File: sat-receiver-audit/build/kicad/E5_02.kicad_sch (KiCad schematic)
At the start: 18 parts, among them J502 UART5 console 3pin locking, J504 Olimex GX16-4 IMU DESIGN pino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, J505 LAB BUS 6pin locking DESIGN, J520 Q6A HDMI Type-A existing port, J522 Q6A factory EDL button functi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, J550 IMU pack cable termination DE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, SW501 EDL recessed momentary NO, U506 LM66100DCKR HDMI5V ideal diode, U520 Wisecoco display/controller a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, U551 TPD4E1U06DBVR, U552 TPD4E1U06DBVR

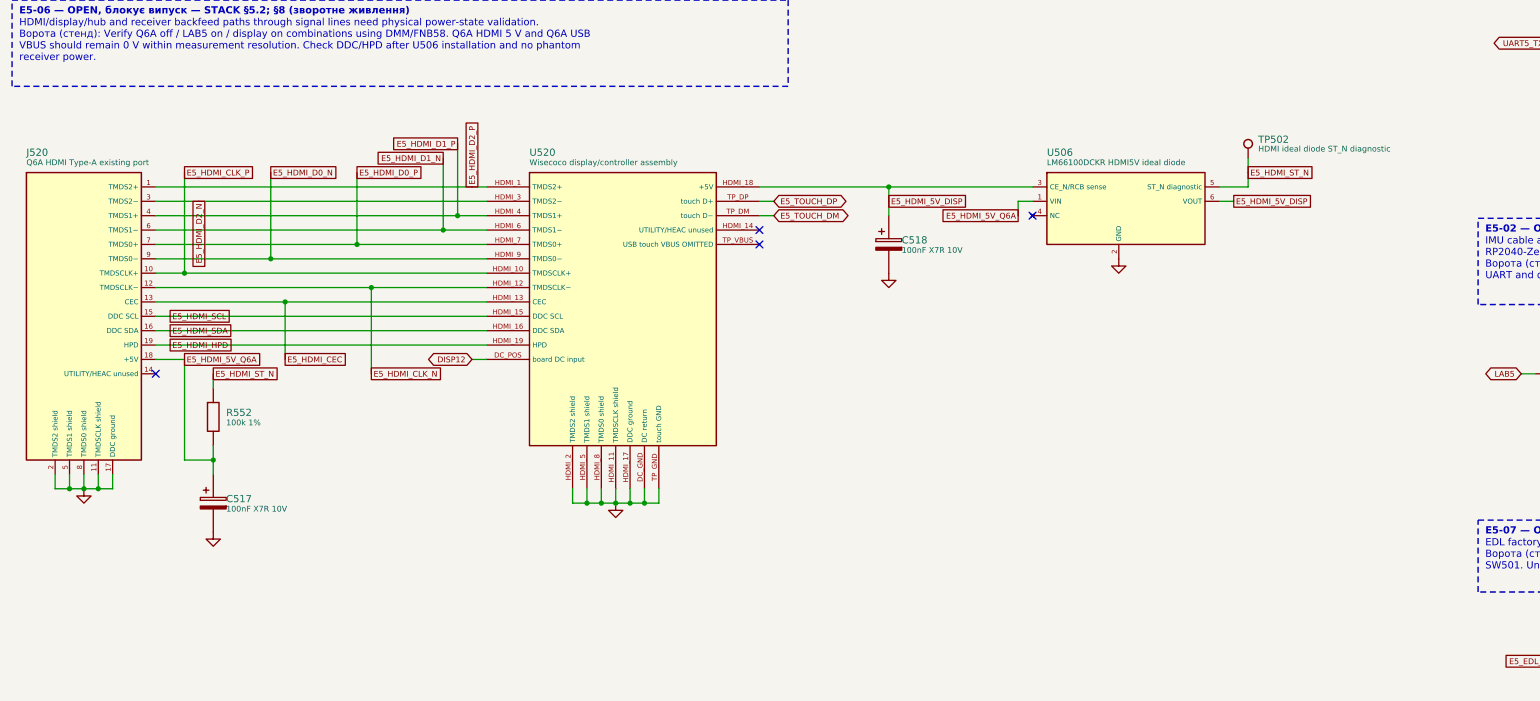
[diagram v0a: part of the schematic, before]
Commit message: Stage 2 integration: CAD and DC_CORE re-freeze from CI run 40094234222; bound-count test and PCB hash lists follow
Co-Authored-By: Claude Opus 5.5 <noreply@anthropic.com>
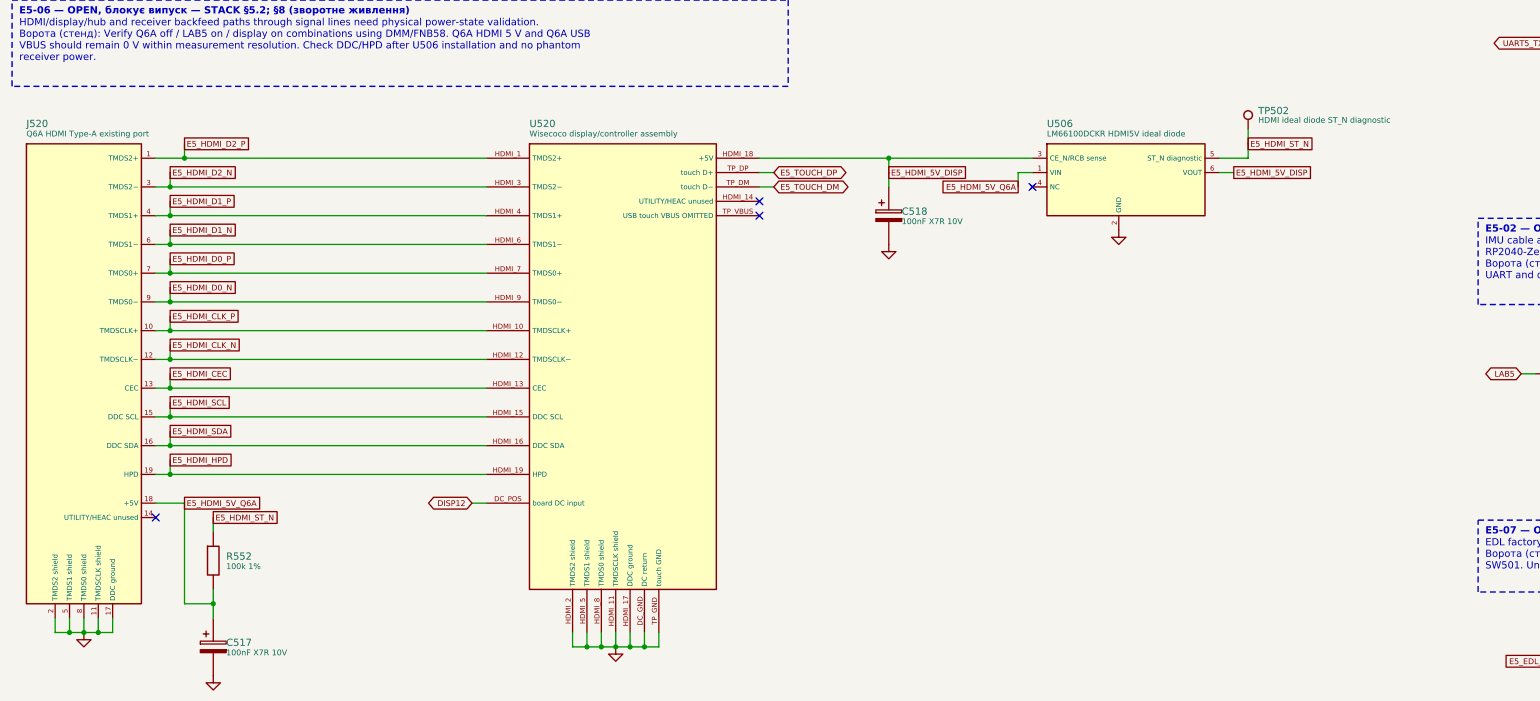
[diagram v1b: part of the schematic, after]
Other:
- moved on the sheet: C517, C518, J520, R552, TP502, U506, U520
